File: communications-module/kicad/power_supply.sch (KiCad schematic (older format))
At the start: 25 parts, among them J1 IDC12, P2 USB_A, P3 USB_A, P4 USB_A, P5 BACKUP, U3 TPS2064, U4 PWR_CONN, U5 TPS2064

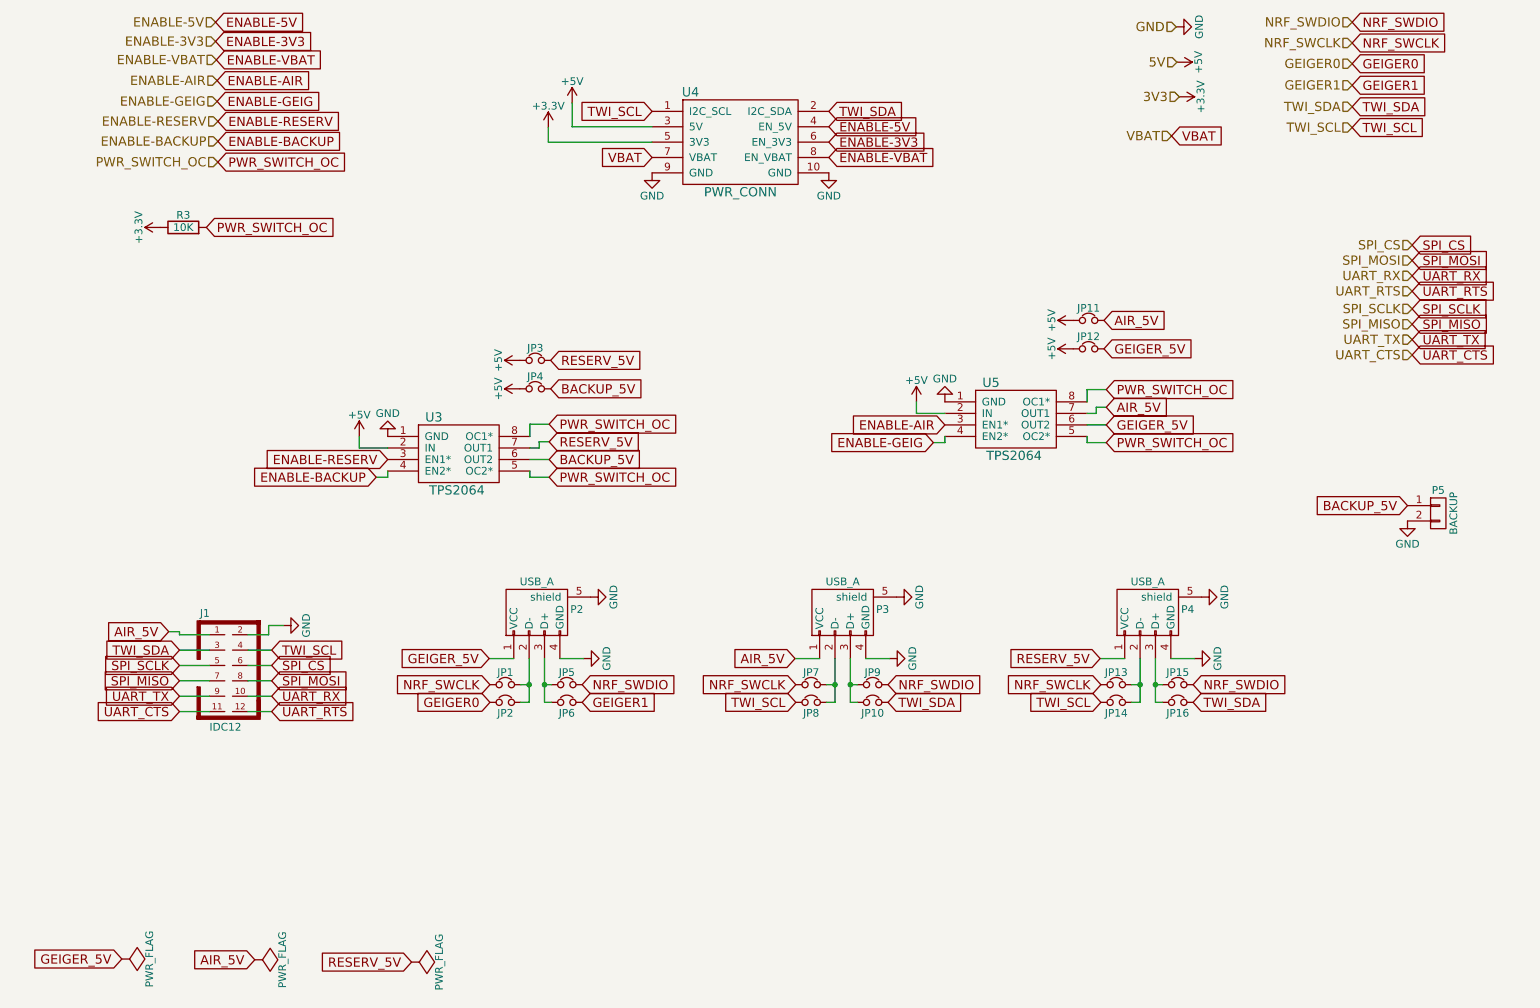
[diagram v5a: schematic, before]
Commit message: Communications Module PCB components placed
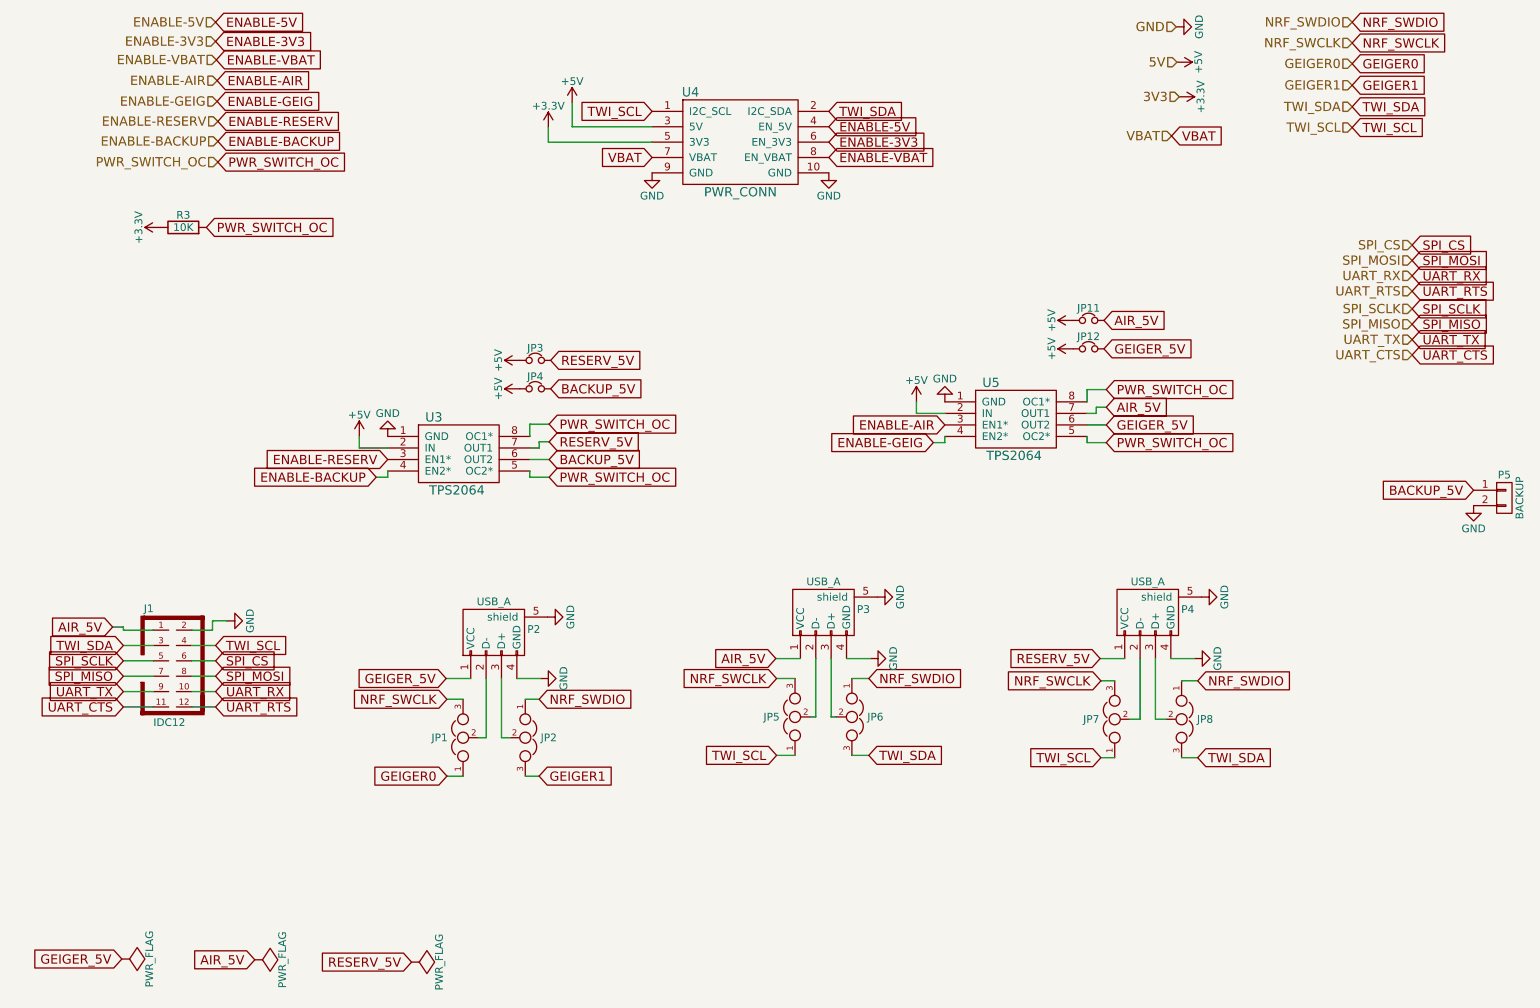
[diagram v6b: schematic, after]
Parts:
- removed JP1, JP10, JP13, JP14, JP15, JP16, JP2, JP5, JP6, JP7, JP8, JP9: Jumper_NC_Small, Socket_Strips:Socket_Strip_Straight_1x02_Pitch2.54mm, symbol Jumper_NC_Small
- added JP1, JP2, JP5, JP6, JP7, JP8: JUMPER3, Socket_Strips:Socket_Strip_Straight_1x03_Pitch2.54mm, symbol JUMPER3
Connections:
- net GEIGER0: now also JP1.1
- net GEIGER1: now also JP2.3
- net NRF_SWCLK: now also JP1.3, JP5.3, JP7.3
- net NRF_SWDIO: now also JP2.1, JP6.1, JP8.1
- net TWI_SCL: now also JP5.1, JP7.1
- net TWI_SDA: now also JP6.3, JP8.3
- net at P3.2 (D-): now also JP5.2
- net at P3.3 (D+): now also JP6.2
- net at P4.2 (D-): now also JP7.2
- net at P4.3 (D+): now also JP8.2
- net at P2.2 (D-): now also JP1.2
- net at P2.3 (D+): now also JP2.2
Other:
- moved on the sheet: J1, P2, P3, P5

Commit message: Communications Module PCB update
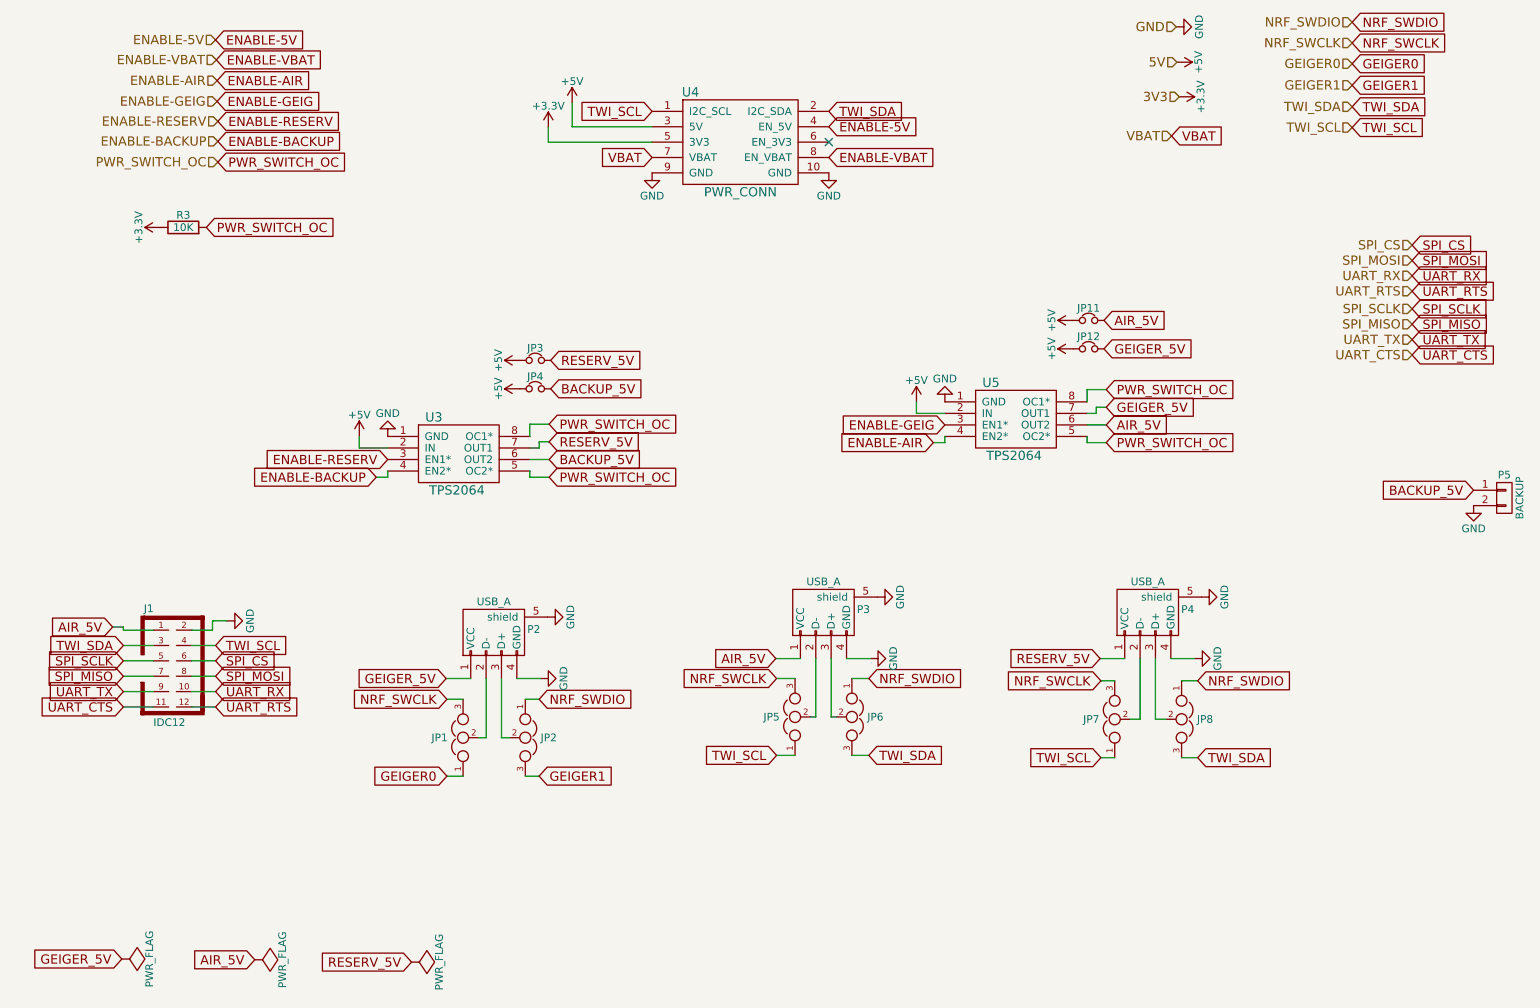
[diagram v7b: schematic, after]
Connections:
- net AIR_5V: now also U5.6 (OUT2); no longer U5.7 (OUT1)
- net ENABLE-AIR: now also U5.4 (EN2*); no longer U5.3 (EN1*)
- net ENABLE-GEIG: now also U5.3 (EN1*); no longer U5.4 (EN2*)
- net GEIGER_5V: now also U5.7 (OUT1); no longer U5.6 (OUT2)
- net ENABLE-3V3: no longer names the net of U4.6 (EN_3V3)
- no-connect marks 0 -> 1
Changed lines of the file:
@@
 TWI_SDA
 $Comp
-L GND #PWR041
+L GND #PWR29
 U 1 1 589845A1
 P 4785 2270
-F 0 "#PWR041" H 4785 2020 50  0001 C CNN
+F 0 "#PWR29" H 4785 2020 50  0001 C CNN
 F 1 "GND" H 4785 2120 50  0000 C CNN
 F 2 "" H 4785 2270 60  0000 C CNN
@@
 $EndComp
 $Comp
-L GND #PWR042
+L GND #PWR30
 U 1 1 589845A7
 P 5935 2270
-F 0 "#PWR042" H 5935 2020 50  0001 C CNN
+F 0 "#PWR30" H 5935 2020 50  0001 C CNN
 F 1 "GND" H 5935 2120 50  0000 C CNN
 F 2 "" H 5935 2270 60  0000 C CNN
@@
 TWI_SCL
 $Comp
-L GND #PWR043
+L GND #PWR32
 U 1 1 589859EA
 P 6250 5030
-F 0 "#PWR043" H 6250 4780 50  0001 C CNN
+F 0 "#PWR32" H 6250 4780 50  0001 C CNN
 F 1 "GND" H 6250 4880 50  0000 C CNN
 F 2 "" H 6250 5030 60  0000 C CNN
@@
 $EndComp
 $Comp
-L GND #PWR044
+L GND #PWR40
 U 1 1 589859F7
 P 8315 5430
-F 0 "#PWR044" H 8315 5180 50  0001 C CNN
+F 0 "#PWR40" H 8315 5180 50  0001 C CNN
 F 1 "GND" H 8315 5280 50  0000 C CNN
 F 2 "" H 8315 5430 60  0000 C CNN
@@
 TWI_SCL
 $Comp
-L GND #PWR045
+L GND #PWR41
 U 1 1 58985A1D
 P 8360 5030
-F 0 "#PWR045" H 8360 4780 50  0001 C CNN
+F 0 "#PWR41" H 8360 4780 50  0001 C CNN
 F 1 "GND" H 8360 4880 50  0000 C CNN
 F 2 "" H 8360 5030 60  0000 C CNN
@@
 $EndComp
 $Comp
-L GND #PWR046
+L GND #PWR25
 U 1 1 58985A2A
 P 4060 5560
-F 0 "#PWR046" H 4060 5310 50  0001 C CNN
+F 0 "#PWR25" H 4060 5310 50  0001 C CNN
 F 1 "GND" H 4060 5410 50  0000 C CNN
 F 2 "" H 4060 5560 60  0000 C CNN
@@
 GEIGER0
 $Comp
-L GND #PWR047
+L GND #PWR26
 U 1 1 58985A50
 P 4105 5160
-F 0 "#PWR047" H 4105 4910 50  0001 C CNN
+F 0 "#PWR26" H 4105 4910 50  0001 C CNN
 F 1 "GND" H 4105 5010 50  0000 C CNN
 F 2 "" H 4105 5160 60  0000 C CNN
@@
 $EndComp
 $Comp
-L GND #PWR048
+L GND #PWR34
 U 1 1 58985A5D
 P 6690 3760
-F 0 "#PWR048" H 6690 3510 50  0001 C CNN
+F 0 "#PWR34" H 6690 3510 50  0001 C CNN
 F 1 "GND" H 6690 3610 50  0000 C CNN
 F 2 "" H 6690 3760 60  0000 C CNN
@@
 	-1   0    0    1
 $EndComp
+Text GLabel 6615 4025 0    60   Input ~ 0
+ENABLE-AIR
+Wire Wire Line
+	6690 3835 6505 3835
+Wire Wire Line
+	6505 3835 6505 3760
 Text GLabel 6690 3910 0    60   Input ~ 0
-ENABLE-AIR
-Wire Wire Line
-	6690 3835 6505 3835
-Wire Wire Line
-	6505 3835 6505 3760
-Text GLabel 6615 4025 0    60   Input ~ 0
 ENABLE-GEIG
 Wire Wire Line
@@
 Wire Wire Line
 	6690 4025 6690 3985
+Text GLabel 7740 3795 2    60   Input ~ 0
+GEIGER_5V
 Text GLabel 7740 3910 2    60   Input ~ 0
-GEIGER_5V
-Text GLabel 7740 3795 2    60   Input ~ 0
 AIR_5V
 Wire Wire Line
@@
 	7615 4025 7740 4025
 $Comp
-L GND #PWR049
+L GND #PWR22
 U 1 1 58985A8F
 P 3065 3985
-F 0 "#PWR049" H 3065 3735 50  0001 C CNN
+F 0 "#PWR22" H 3065 3735 50  0001 C CNN
 F 1 "GND" H 3065 3835 50  0000 C CNN
 F 2 "" H 3065 3985 60  0000 C CNN
@@
 RESERV_5V
 $Comp
-L GND #PWR050
+L GND #PWR31
 U 1 1 58985AAE
 P 6205 5430
-F 0 "#PWR050" H 6205 5180 50  0001 C CNN
+F 0 "#PWR31" H 6205 5180 50  0001 C CNN
 F 1 "GND" H 6205 5280 50  0000 C CNN
 F 2 "" H 6205 5430 60  0000 C CNN
@@
 $EndComp
 $Comp
-L +5V #PWR051
+L +5V #PWR23
 U 1 1 58985ABE
 P 3925 3490
-F 0 "#PWR051" H 3925 3340 50  0001 C CNN
+F 0 "#PWR23" H 3925 3340 50  0001 C CNN
 F 1 "+5V" H 3925 3630 50  0000 C CNN
 F 2 "" H 3925 3490 60  0000 C CNN
@@
 $EndComp
 $Comp
-L +5V #PWR052
+L +5V #PWR35
 U 1 1 58985AD9
 P 7525 3230
-F 0 "#PWR052" H 7525 3080 50  0001 C CNN
+F 0 "#PWR35" H 7525 3080 50  0001 C CNN
 F 1 "+5V" H 7525 3370 50  0000 C CNN
 F 2 "" H 7525 3230 60  0000 C CNN
@@
 $EndComp
 $Comp
-L +5V #PWR053
+L +5V #PWR36
 U 1 1 58985AE6
 P 7525 3415
-F 0 "#PWR053" H 7525 3265 50  0001 C CNN
+F 0 "#PWR36" H 7525 3265 50  0001 C CNN
 F 1 "+5V" H 7525 3555 50  0000 C CNN
 F 2 "" H 7525 3415 60  0000 C CNN
@@
 5V
 $Comp
-L +5V #PWR054
+L +5V #PWR38
 U 1 1 58988CC2
 P 8200 1550
-F 0 "#PWR054" H 8200 1400 50  0001 C CNN
+F 0 "#PWR38" H 8200 1400 50  0001 C CNN
 F 1 "+5V" H 8200 1690 50  0000 C CNN
 F 2 "" H 8200 1550 60  0000 C CNN
@@
 $EndComp
 $Comp
-L +3.3V #PWR055
+L +3.3V #PWR39
 U 1 1 58989B65
 P 8215 1775
-F 0 "#PWR055" H 8215 1625 50  0001 C CNN
+F 0 "#PWR39" H 8215 1625 50  0001 C CNN
 F 1 "+3.3V" H 8215 1915 50  0000 C CNN
 F 2 "" H 8215 1775 60  0000 C CNN
@@
 TWI_SCL
 $Comp
-L +5V #PWR056
+L +5V #PWR28
 U 1 1 589845B4
 P 4265 1815
-F 0 "#PWR056" H 4265 1665 50  0001 C CNN
+F 0 "#PWR28" H 4265 1665 50  0001 C CNN
 F 1 "+5V" H 4265 1955 50  0000 C CNN
 F 2 "" H 4265 1815 60  0000 C CNN
@@
 $EndComp
 $Comp
-L +3.3V #PWR057
+L +3.3V #PWR27
 U 1 1 589845AE
 P 4110 1975
-F 0 "#PWR057" H 4110 1825 50  0001 C CNN
+F 0 "#PWR27" H 4110 1825 50  0001 C CNN
 F 1 "+3.3V" H 4110 2115 50  0000 C CNN
 F 2 "" H 4110 1975 60  0000 C CNN
@@
 BACKUP_5V
 $Comp
-L GND #PWR058
+L GND #PWR42
 U 1 1 589977EF
 P 10130 4435
-F 0 "#PWR058" H 10130 4185 50  0001 C CNN
+F 0 "#PWR42" H 10130 4185 50  0001 C CNN
 F 1 "GND" H 10130 4285 50  0000 C CNN
 F 2 "" H 10130 4435 60  0000 C CNN
@@
 AIR_5V
 $Comp
-L GND #PWR059
+L GND #PWR37
 U 1 1 58A00F9B
 P 8195 1320
-F 0 "#PWR059" H 8195 1070 50  0001 C CNN
+F 0 "#PWR37" H 8195 1070 50  0001 C CNN
 F 1 "GND" H 8195 1170 50  0000 C CNN
 F 2 "" H 8195 1320 60  0000 C CNN
@@
 $EndComp
 $Comp
-L +3.3V #PWR060
+L +3.3V #PWR19
 U 1 1 58999FE9
 P 1585 2625
-F 0 "#PWR060" H 1585 2475 50  0001 C CNN
+F 0 "#PWR19" H 1585 2475 50  0001 C CNN
 F 1 "+3.3V" H 1585 2765 50  0000 C CNN
 F 2 "" H 1585 2625 60  0000 C CNN
@@
 SPI_SCLK
 $Comp
-L GND #PWR061
+L GND #PWR20
 U 1 1 58A15D45
 P 2020 5185
-F 0 "#PWR061" H 2020 4935 50  0001 C CNN
+F 0 "#PWR20" H 2020 4935 50  0001 C CNN
 F 1 "GND" H 2020 5035 50  0000 C CNN
 F 2 "" H 2020 5185 60  0000 C CNN
@@
 ENABLE-AIR
 $Comp
-L +5V #PWR062
+L +5V #PWR21
 U 1 1 58985A95
 P 2880 3985
-F 0 "#PWR062" H 2880 3835 50  0001 C CNN
+F 0 "#PWR21" H 2880 3835 50  0001 C CNN
 F 1 "+5V" H 2880 4125 50  0000 C CNN
 F 2 "" H 2880 3985 60  0000 C CNN
@@
 $EndComp
 $Comp
-L +5V #PWR063
+L +5V #PWR24
 U 1 1 58985ACB
 P 3925 3675
-F 0 "#PWR063" H 3925 3525 50  0001 C CNN
+F 0 "#PWR24" H 3925 3525 50  0001 C CNN
 F 1 "+5V" H 3925 3815 50  0000 C CNN
 F 2 "" H 3925 3675 60  0000 C CNN
@@
 BACKUP_5V
 $Comp
-L +5V #PWR064
+L +5V #PWR33
 U 1 1 58985A63
 P 6505 3760
-F 0 "#PWR064" H 6505 3610 50  0001 C CNN
+F 0 "#PWR33" H 6505 3610 50  0001 C CNN
 F 1 "+5V" H 6505 3900 50  0000 C CNN
 F 2 "" H 6505 3760 60  0000 C CNN
@@
 Text GLabel 5935 1970 2    60   Input ~ 0
 ENABLE-5V
-Text GLabel 5935 2070 2    60   Input ~ 0
-ENABLE-3V3
 Text GLabel 5935 2170 2    60   Input ~ 0
 ENABLE-VBAT
-Text GLabel 1945 1290 2    60   Input ~ 0
+Text GLabel 1945 1405 2    60   Input ~ 0
 ENABLE-5V
-Text GLabel 1945 1415 2    60   Input ~ 0
-ENABLE-3V3
 Text GLabel 1950 1535 2    60   Input ~ 0
 ENABLE-VBAT
 Text HLabel 1950 1535 0    60   Input ~ 0
 ENABLE-VBAT
-Text HLabel 1945 1415 0    60   Input ~ 0
-ENABLE-3V3
-Text HLabel 1945 1290 0    60   Input ~ 0
+Text HLabel 1945 1405 0    60   Input ~ 0
 ENABLE-5V
 Text GLabel 1335 7385 0    60   Input ~ 0
@@
 RESERV_5V
 $Comp
-L PWR_FLAG #FLG065
+L PWR_FLAG #FLG22
 U 1 1 589AC172
 P 1335 7385
-F 0 "#FLG065" H 1335 7480 50  0001 C CNN
+F 0 "#FLG22" H 1335 7480 50  0001 C CNN
 F 1 "PWR_FLAG" H 1335 7565 50  0000 C CNN
 F 2 "" H 1335 7385 60  0000 C CNN
@@
 $EndComp
 $Comp
-L PWR_FLAG #FLG066
+L PWR_FLAG #FLG23
 U 1 1 589AC39B
 P 2200 7390
-F 0 "#FLG066" H 2200 7485 50  0001 C CNN
+F 0 "#FLG23" H 2200 7485 50  0001 C CNN
 F 1 "PWR_FLAG" H 2200 7570 50  0000 C CNN
 F 2 "" H 2200 7390 60  0000 C CNN
@@
 $EndComp
 $Comp
-L PWR_FLAG #FLG067
+L PWR_FLAG #FLG24
 U 1 1 589AC824
 P 3220 7405
-F 0 "#FLG067" H 3220 7500 50  0001 C CNN
+F 0 "#FLG24" H 3220 7500 50  0001 C CNN
 F 1 "PWR_FLAG" H 3220 7585 50  0000 C CNN
 F 2 "" H 3220 7405 60  0000 C CNN
@@
 Wire Wire Line
 	8230 6075 8335 6075
+NoConn ~ 5935 2070
 $EndSCHEMATC
